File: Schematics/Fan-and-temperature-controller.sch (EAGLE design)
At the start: 33 parts, among them IC1 MEGA8-P, IC2 LM35CZ, T1 BC547, T2 BC547, T3 BC547, X1 DB9-F

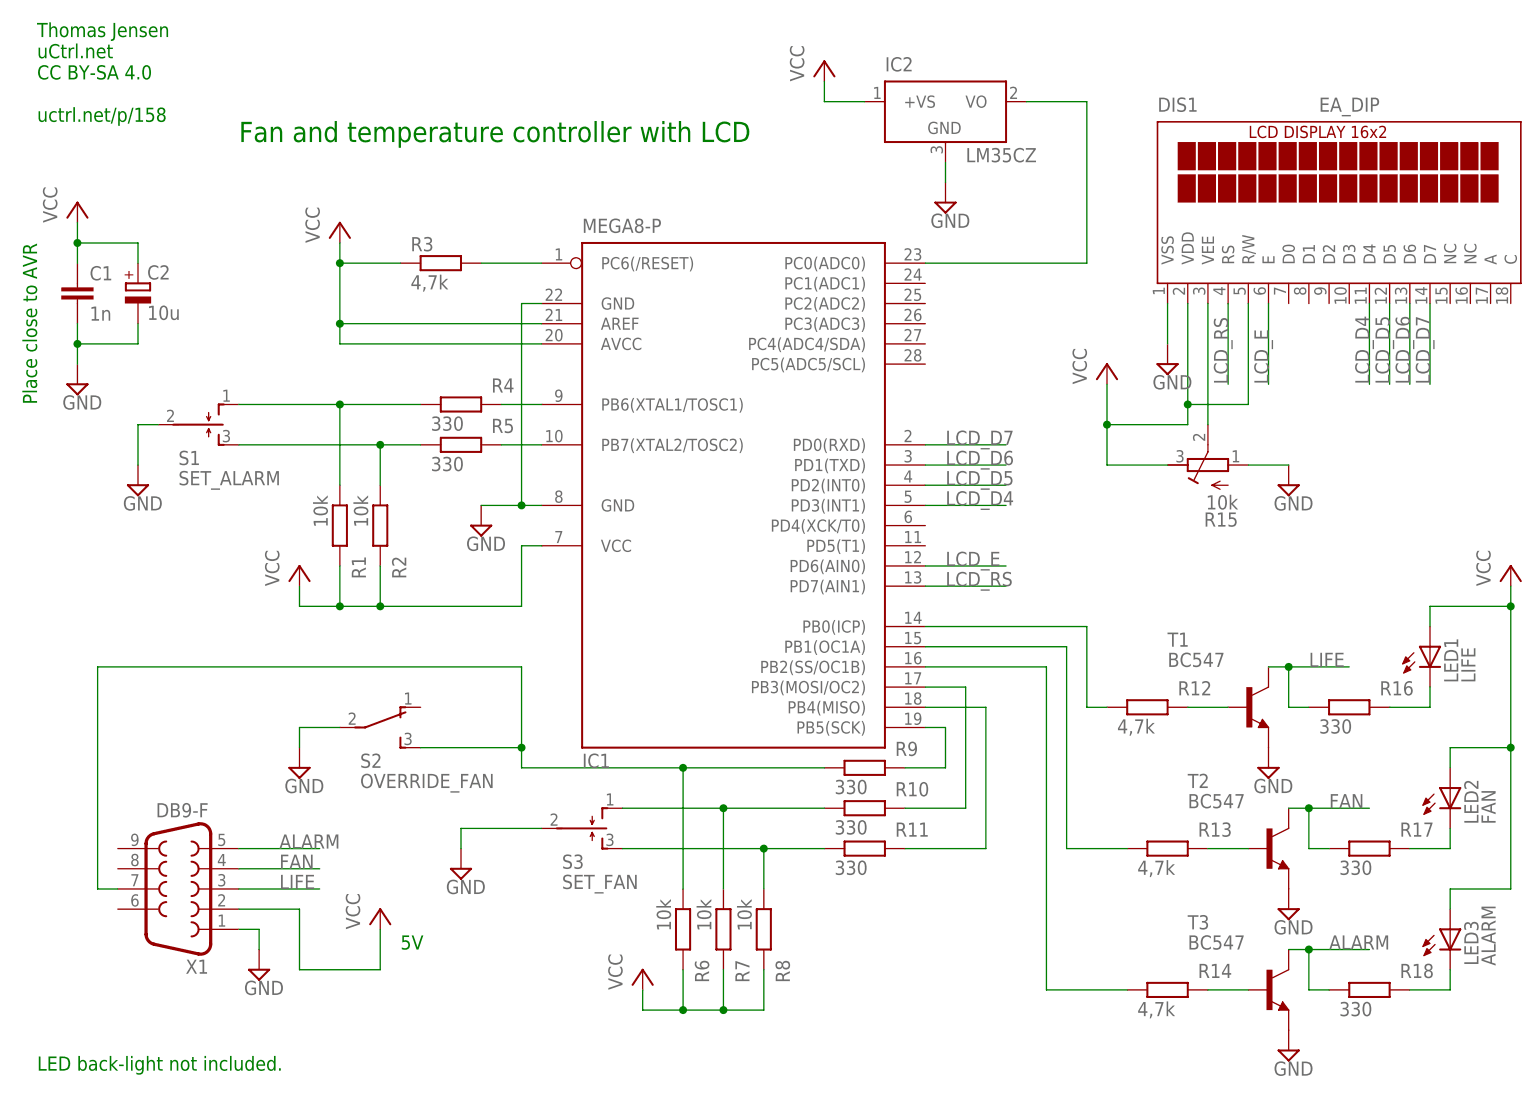
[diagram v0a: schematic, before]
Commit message: move schematic diagrams
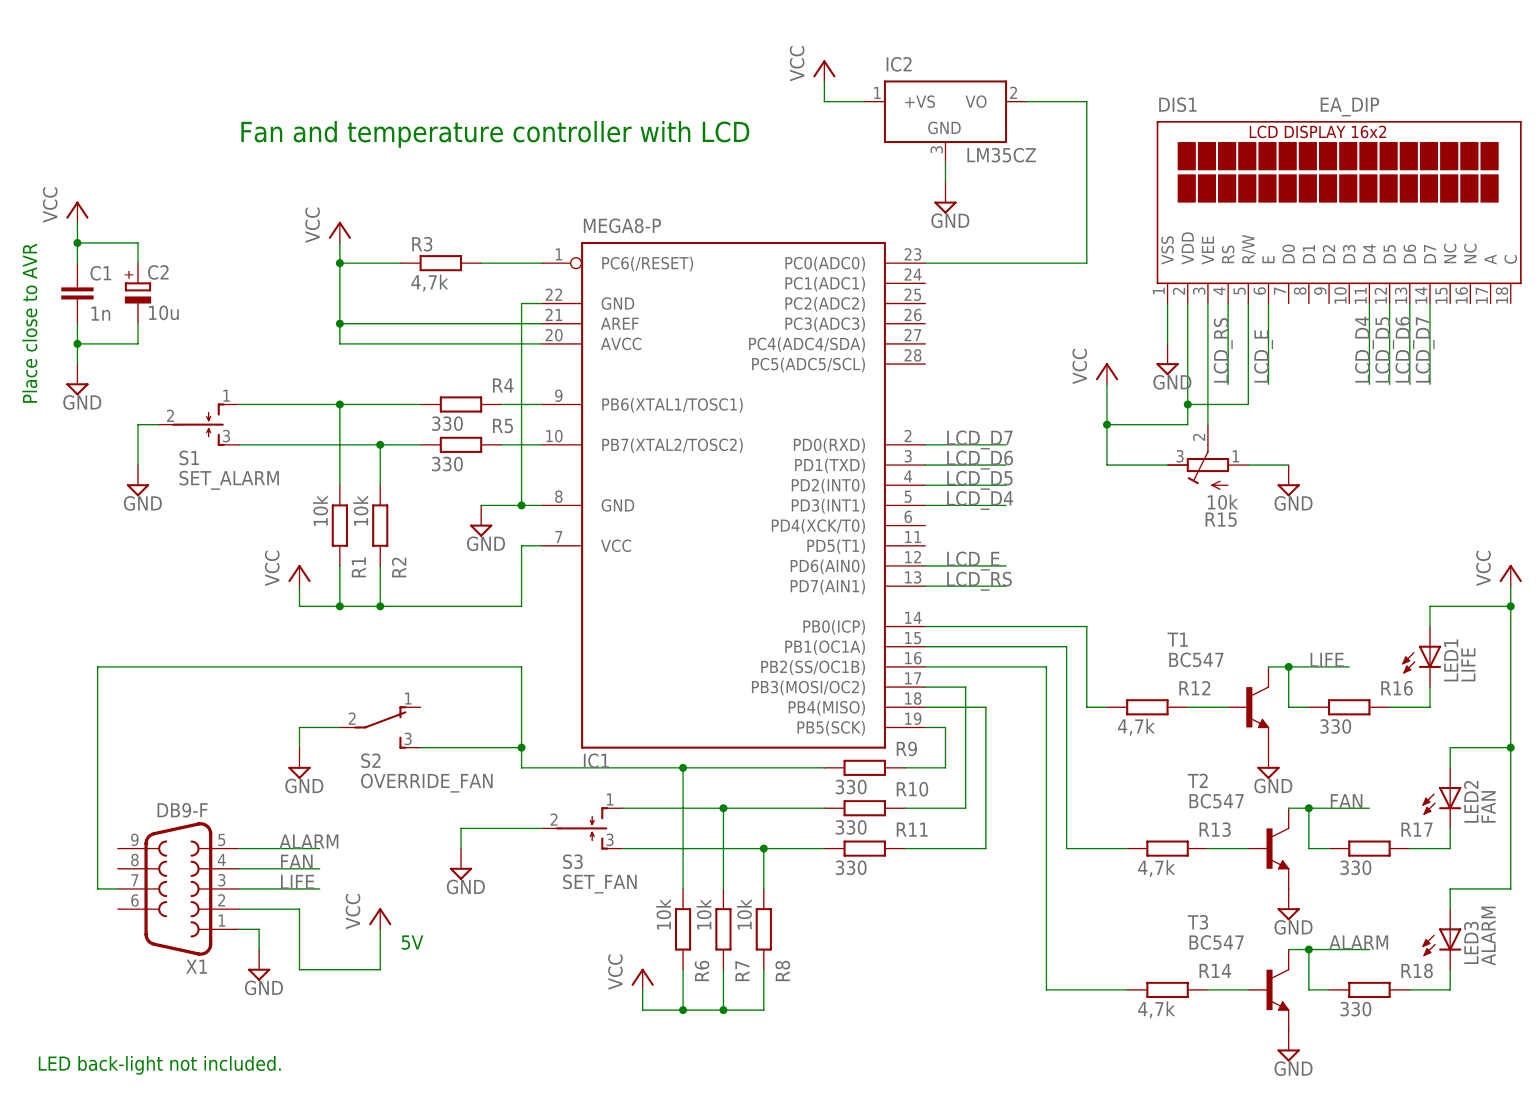
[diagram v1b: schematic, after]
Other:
- note removed: "Thomas Jensen uCtrl.net CC BY-SA 4.0 uctrl.net/p/158"
